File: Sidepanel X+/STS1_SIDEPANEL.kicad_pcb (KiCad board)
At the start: 2 copper layers, 82.8 x 100 mm, 39 parts, among them IC1 TMP112AQDRLRQ1, J1 Conn_01x08, U1 GUVA-C32SM, U11 INA180A4

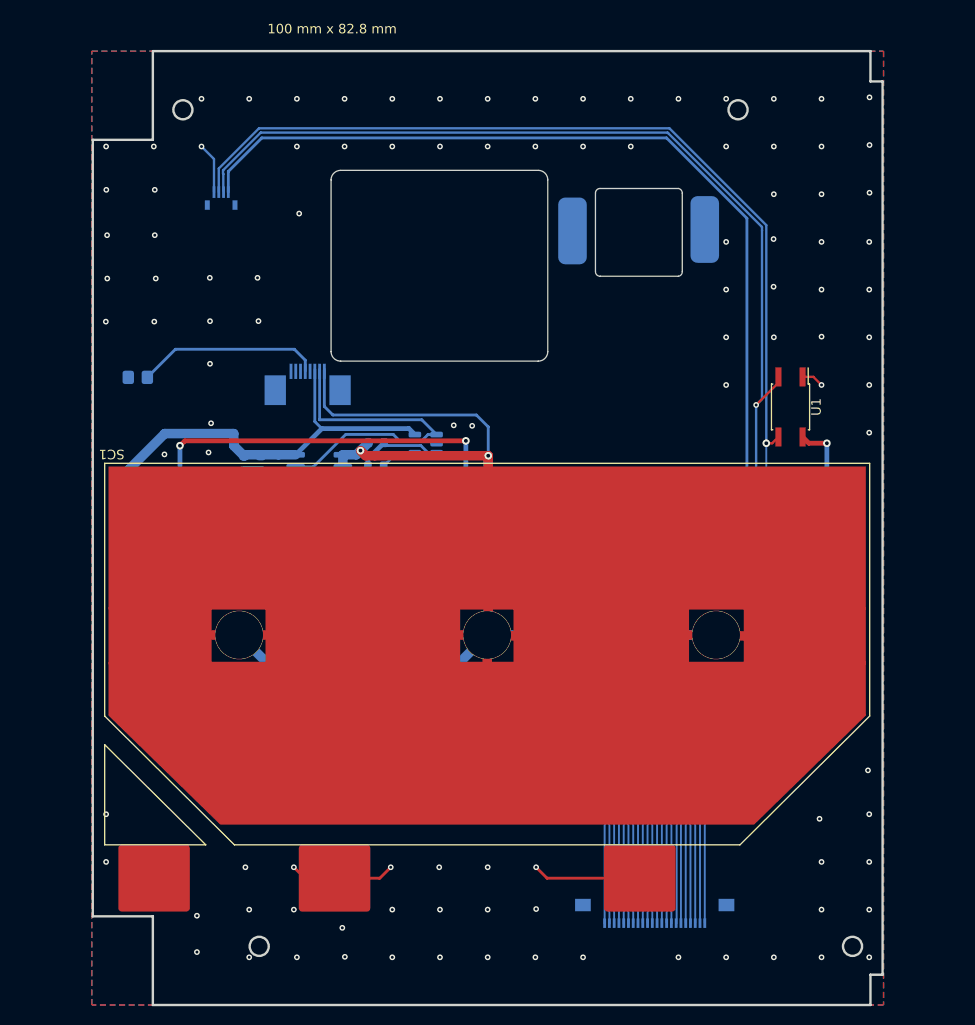
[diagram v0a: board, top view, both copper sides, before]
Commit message: fix for the issues: #19, #18 moved some components from the edge away to avoid collisions with the new structure
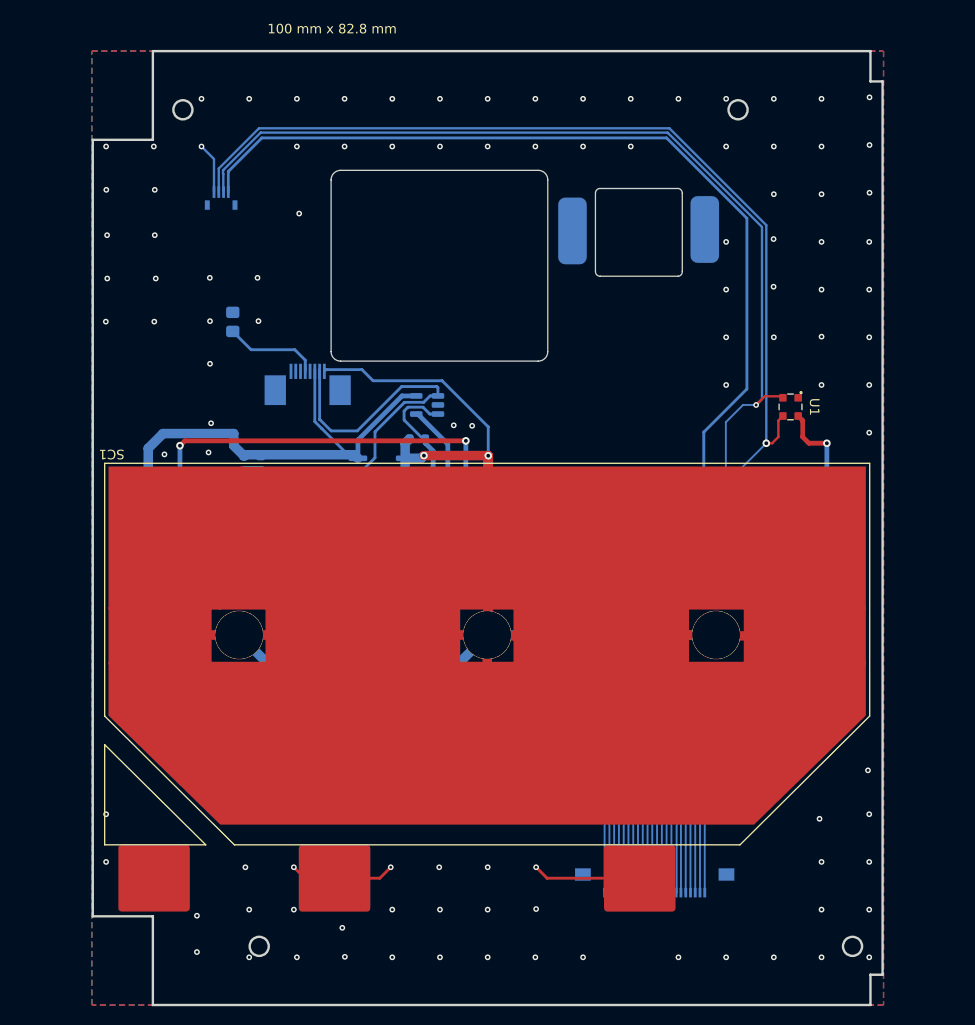
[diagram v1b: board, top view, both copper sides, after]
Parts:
- U1: footprint Package_SO:SO-4_4.4x3.6mm_P2.54mm -> STS_UV:OLGA 2mm x 2,3mm
- moved TH1 11.5 mm to (98.3, 67.9), turned to 90 degrees
- moved C_IN1 6.76 mm to (120.0, 85.5)
- moved R51 6.74 mm to (120.0, 83.5)
- moved CUR1 6.54 mm to (113.9, 84.1)
- moved C1 4.93 mm to (157.9, 94.6)
- moved RIC1 4.93 mm to (149.9, 89.3)
- moved RIC2 4.93 mm to (149.9, 91.3)
- moved RU1 4.93 mm to (149.9, 95.6)
- moved RU2 4.93 mm to (149.9, 93.6)
- moved C2 4.93 mm to (157.9, 90.4)
- moved IC1 4.93 mm to (154.3, 94.2)
- moved R41 4.33 mm to (117.6, 80.2)
- moved U11 4.05 mm to (118.7, 76.6)
- moved edu_con1 3.20 mm to (142.5, 125.7)
- moved C21 2.10 mm to (96.5, 94.5)
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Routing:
- net /TEMP+: track 19.4 -> 10.0 mm
- net /SC1_V+: track 213.6 -> 205.7 mm
- net /MPPT1: track 75.0 -> 82.1 mm
- net /SolarMPPT/CUR1_OUT(1): track 33.5 -> 38.8 mm
- net GND: track 57.5 -> 61.9 mm
- net Net-(cam1-Pad16): track 18.6 -> 15.4 mm
- net Net-(cam1-Pad9): track 18.6 -> 15.4 mm
- net Net-(cam1-Pad8): track 18.6 -> 15.4 mm
- net Net-(cam1-Pad7): track 18.6 -> 15.4 mm
- net Net-(cam1-Pad6): track 18.6 -> 15.4 mm
- net Net-(cam1-Pad5): track 18.6 -> 15.4 mm
- net Net-(cam1-Pad4): track 18.6 -> 15.4 mm
- net Net-(cam1-Pad3): track 18.6 -> 15.4 mm
- net Net-(cam1-Pad22): track 18.6 -> 15.4 mm
- net Net-(cam1-Pad21): track 18.6 -> 15.4 mm
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
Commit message: Changed the layout of all the sidepanel PCBs to mitigate the problems that arised from the bad previous design.
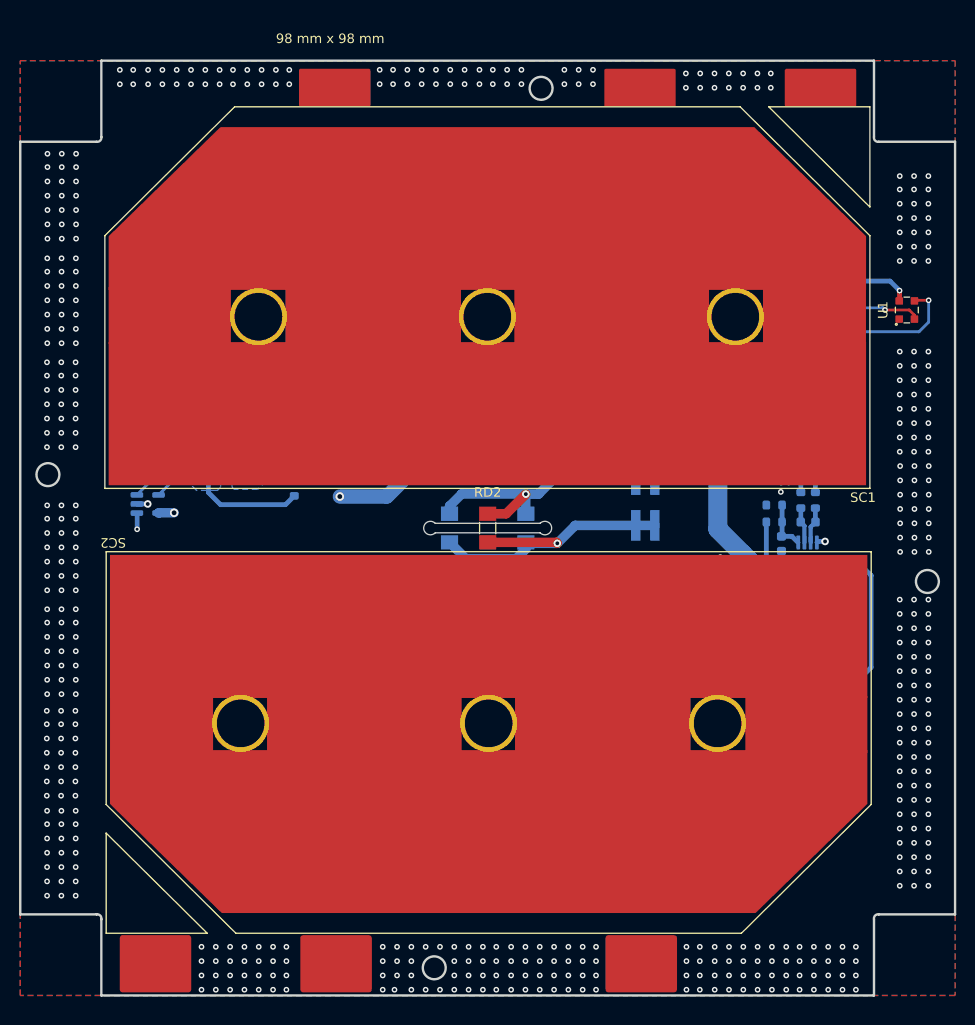
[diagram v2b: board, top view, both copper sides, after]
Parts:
- removed ? (x2): , 
- removed C2, CF1: 1u, Capacitor_SMD:C_0603_1608Metric
- removed COUT11: 4u7, Capacitor_SMD:C_0603_1608Metric
- removed COUT21, C_CUR21, C_IN1: 10u, Capacitor_SMD:C_0603_1608Metric
- removed CUR1: TMCS1101A3BQDT, Package_SO:SOIC-8_3.9x4.9mm_P1.27mm
- removed C_41, C_CUR11: 100n, Capacitor_SMD:C_0603_1608Metric
- removed D1: PMEG2020EH, Diode_SMD:D_SOD-123F
- removed DOUT1: SMM4F5.0, SamacSys:STMITE
- removed L_IN1: 10u, STS_Inductor_SMD:IND_XAL6060-103MEC
- removed RF11, RF21: 1k, Resistor_SMD:R_0603_1608Metric
- removed RIC1, RIC2: 4k7, Resistor_SMD:R_0603_1608Metric
- removed RS1: 0R01, Resistor_SMD:R_0603_1608Metric
- removed cam1, edu_con1: 54548-2271, STS_Connector:545482271
- added C11: 10u, Capacitor_SMD:C_0603_1608Metric, B.Cu at (95.4, 77.0)
- added C12: 10u, Capacitor_SMD:C_0603_1608Metric, B.Cu at (155.0, 104.4)
- added C22: 100n, Capacitor_SMD:C_0603_1608Metric, B.Cu at (161.9, 95.2)
- added C31: 1n, Capacitor_SMD:C_0603_1608Metric, B.Cu at (108.4, 77.8)
- added C32: 1n, Capacitor_SMD:C_0603_1608Metric, B.Cu at (155.8, 91.1)
- added C41: 4u7, Capacitor_SMD:C_0603_1608Metric, B.Cu at (101.3, 75.4)
- added C42: 1u, Capacitor_SMD:C_0603_1608Metric, B.Cu at (158.6, 88.9)
- added C51: 1u, Capacitor_SMD:C_0603_1608Metric, B.Cu at (111.4, 80.3)
- added C52: 4u7, Capacitor_SMD:C_0603_1608Metric, B.Cu at (153.5, 98.0)
- added C61: 10u, Capacitor_SMD:C_0603_1608Metric, B.Cu at (106.5, 73.1)
- added C62: 10u, Capacitor_SMD:C_0603_1608Metric, B.Cu at (151.5, 93.7)
- added D11: PMEG2020EH, Diode_SMD:D_SOD-123F, B.Cu at (101.6, 77.4)
- added D12: PMEG2020EH, Diode_SMD:D_SOD-123F, B.Cu at (155.5, 98.8)
- added D21: SMM4F5.0, STS_semiconductor:DIO_SMM4F5.0A-TR, B.Cu at (102.9, 73.3)
- added D22: SMM4F5.0, STS_semiconductor:DIO_SMM4F5.0A-TR, B.Cu at (151.5, 98.7)
- added J3: Conn_02x02_Odd_Even, STS_Connector:M808280442, B.Cu at (141.5, 86.8)
- added L1: 10u, STS_Inductor_SMD:IND_XAL6060-103MEC, B.Cu at (97.7, 82.2)
- added L_IN2: 10u, STS_Inductor_SMD:IND_XAL6060-103MEC, B.Cu at (160.4, 102.8)
- added MPPT2: SPV1040TTR, Package_SO:TSSOP-8_4.4x3mm_P0.65mm, B.Cu at (158.5, 93.9)
- added R12: 10m, Resistor_SMD:R_0603_1608Metric, B.Cu at (157.6, 107.9)
- added R22: 1k, Resistor_SMD:R_0603_1608Metric, B.Cu at (161.9, 93.7)
- added R32: 1k, Resistor_SMD:R_0603_1608Metric, B.Cu at (159.4, 86.6)
- added R42: 1k, Resistor_SMD:R_0603_1608Metric, B.Cu at (157.8, 86.6)
- added R52: 0R01, Resistor_SMD:R_0603_1608Metric, B.Cu at (153.8, 94.5)
- added R61: 1M, Resistor_SMD:R_0603_1608Metric, B.Cu at (111.0, 76.9)
- added R62: 1M, Resistor_SMD:R_0603_1608Metric, B.Cu at (155.0, 88.9)
- added R71: 330k, Resistor_SMD:R_0603_1608Metric, B.Cu at (112.5, 76.9)
- added R72: 330k, Resistor_SMD:R_0603_1608Metric, B.Cu at (155.0, 87.1)
- added RD1: 22R, Resistor_SMD:R_MiniMELF_MMA-0204, B.Cu at (121.0, 89.5)
- added RD2: 22R, Resistor_SMD:R_MiniMELF_MMA-0204, F.Cu at (125.0, 89.5)
- added RD3: 22R, Resistor_SMD:R_MiniMELF_MMA-0204, B.Cu at (129.0, 89.5)
- added SC2: Solar_Cell, STS_solder:3G30A_40x80_Z_SC2, F.Cu at (125.1, 112.0)
- added U12: INA180A4, Package_TO_SOT_SMD:SOT-23-5, B.Cu at (161.6, 111.2)
- C21: value 1n -> 100n
- J1: value Conn_01x08 -> Conn_01x10; footprint STS_Connector:SAMTEC_ZF5S-08-01-T-WT -> STS_connector:SAMTEC_ZF5S-08-01-T-WT
- Outline1: footprint USER_OUTLINE:OUTLINE_SidepanelX+ -> STS_Sidepanels_Outline:OUTLINE_SidepanelX+
- R11: value 1M -> 10m
- R21: value 330k -> 1k
- R41: value 0 -> 1k
- R51: value 10m -> 0R01
- SC1: footprint STS_solder:3G30A_40x80 -> STS_solder:3G30A_40x80_Z_SC1
- U1: footprint STS_UV:OLGA 2mm x 2,3mm -> STS_UV:OLGA
- UV1: footprint STS_Connector:5014610491 -> STS_connector:5014610491
- moved UV1 68.0 mm to (161.8, 75.8), turned to 0 degrees
- moved TH1 52.8 mm to (150.4, 76.1), turned to 0 degrees
- moved SC1 37.4 mm to (125.0, 65.3), turned to 0 degrees
- moved C1 32.2 mm to (163.1, 62.8)
- moved U11 31.1 mm to (89.4, 87.0), turned to 0 degrees
- moved RU2 30.6 mm to (162.3, 65.6)
- moved IC1 27.0 mm to (161.6, 68.2), turned to 90 degrees
- moved RU1 26.9 mm to (161.3, 71.2)
- moved J1 26.0 mm to (132.1, 75.0), turned to 0 degrees
- moved R51 16.7 mm to (105.4, 75.5), turned to 180 degrees
- moved R21 16.3 mm to (104.7, 85.3), turned to -90 degrees
- moved U1 15.9 mm to (168.9, 66.6), turned to 90 degrees
- moved C21 13.7 mm to (104.0, 83.0), turned to 180 degrees
- moved R11 12.8 mm to (92.2, 81.7), turned to 0 degrees
- moved MPPT1 11.6 mm to (106.0, 80.4), turned to 0 degrees
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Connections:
- C21 pad 1: Net-(C21-Pad1) -> GND
- C21 pad 2: GND -> Net-(MPPT1-MPP-SET)
- J1 pad S1: (no net) -> unconnected-(J1-Pin_9-PadS1)
- J1 pad S2: (no net) -> unconnected-(J1-Pin_10-PadS2)
- MPPT1 pad 1: Net-(C_41-Pad2) -> Net-(MPPT1-MPP-SET)
- MPPT1 pad 3: /SolarMPPT/MPPT1_IN -> Net-(D11-A)
- MPPT1 pad 5: Net-(C21-Pad1) -> Net-(MPPT1-VCTRL)
- MPPT1 pad 6: Net-(CF1-Pad1) -> Net-(MPPT1-ICTRL_MINUS)
- MPPT1 pad 7: Net-(CF1-Pad2) -> Net-(MPPT1-ICTRL_PLUS)
- MPPT1 pad 8: Net-(C_41-Pad2) -> Net-(MPPT1-MPP-SET)
- R11 pad 1: Net-(C21-Pad1) -> /SC1_V+
- R11 pad 2: /MPPT1 -> /SolarMPPT/CUR1_OUT
- R21 pad 1: GND -> Net-(MPPT1-MPP-SET)
- R21 pad 2: Net-(C21-Pad1) -> /SolarMPPT/CUR1_OUT
- R31 pad 1: Net-(C_41-Pad2) -> /SolarMPPT/MPPT1_OUT
- R31 pad 2: /SolarMPPT/CUR1_OUT(1) -> Net-(MPPT1-ICTRL_PLUS)
- R41 pad 1: /SC1_V+ -> /MPPT1
- R41 pad 2: /SolarMPPT/CUR1_OUT -> Net-(MPPT1-ICTRL_MINUS)
- R51 pad 1: /SolarMPPT/CUR1_OUT -> /MPPT1
- R51 pad 2: /SolarMPPT/CUR1_OUT(1) -> /SolarMPPT/MPPT1_OUT
- U11 pad 3: /SolarMPPT/CUR1_OUT -> /SC1_V+
- U11 pad 4: /SolarMPPT/CUR1_OUT(1) -> /SolarMPPT/CUR1_OUT
- UV1 pad 4: GND -> unconnected-(UV1-Pad4)
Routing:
- net /SC1_V+: track 205.7 -> 47.8 mm, vias 2 -> 0
- net /+3V3: track 137.0 -> 25.8 mm
- net /SCL: track 112.3 -> 21.2 mm
- net /SDA: track 113.3 -> 24.8 mm, vias 1 -> 2
- net /MPPT2: track 0.00 -> 77.8 mm, vias 0 -> 3
- net /SolarMPPT/MPPT1_OUT: track 86.7 -> 24.0 mm
- net /SC2_I+: track 0.00 -> 54.5 mm, vias 0 -> 2
- net /SC2_V+: track 0.00 -> 45.9 mm, vias 0 -> 1
- net GND: track 61.9 -> 21.7 mm, vias 105 -> 703
- net /SolarMPPT/CUR1_OUT(1): track 38.8 -> 0.00 mm
- net /AntennaDeployment/ANT_DEPLOY-: track 0.00 -> 31.5 mm, vias 0 -> 1
- net /AntennaDeployment/ANT_DEPLOY+: track 0.00 -> 30.4 mm, vias 0 -> 1
- net /SolarMPPT/CUR2_OUT: track 0.00 -> 21.9 mm
- net /SolarMPPT/MPPT1_IN: track 21.4 -> 0.00 mm
- net /SolarMPPT/MPPT2_OUT: track 0.00 -> 20.7 mm, vias 0 -> 2
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- added copper zone on B.Cu, net /MPPT1
- added copper zone on B.Cu, net /MPPT2
- added copper zone on B.Cu, net /SC1_V+
- added copper zone on B.Cu, net /SC2_V+
- added copper zone on B.Cu, net /SolarMPPT/CUR1_OUT
- added copper zone on B.Cu, net /SolarMPPT/CUR2_OUT
- added copper zone on B.Cu, net /SolarMPPT/MPPT2_OUT
- added copper zone on In1.Cu, net GND
- added copper zone on In2.Cu, net GND
- added copper zone on B.Cu, net Net-(D11-A)
- added copper zone on B.Cu, net Net-(D12-A)
- removed copper zone on B.Cu, net /SolarMPPT/MPPT1_IN
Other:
- board size 82.8 x 100 mm -> 98 x 98 mm
- copper layers 2 -> 4
- board text added: "98 mm x 98 mm"
- board text added: "Y"
- board text added: "Z"
- board text removed: "100 mm x 82.8 mm"

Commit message: Added a  separate ground for the EDU  sensors and did  some small changes for ordering.
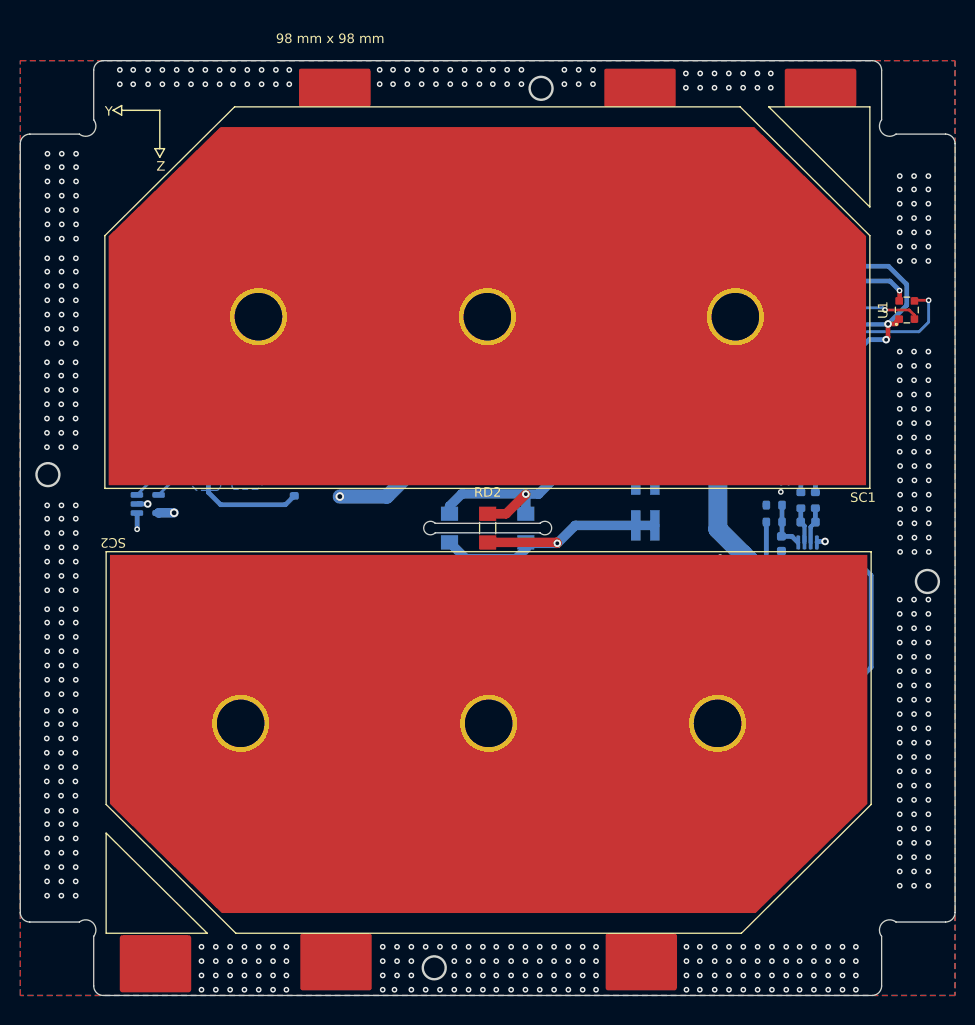
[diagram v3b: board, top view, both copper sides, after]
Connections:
- C1 pad 2: GND -> GND1
- IC1 pad 2: GND -> GND1
- IC1 pad 3: GND -> GND1
- U1 pad 1: GND -> GND1
- UV1 pad 4: unconnected-(UV1-Pad4) -> GND1
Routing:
- net GND1: track 0.00 -> 31.9 mm, vias 0 -> 2
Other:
- outline, holes or cut-outs redrawn

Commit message: Commit before the order.
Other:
- board text added: "V 2.5"
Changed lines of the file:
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@@
       (drillshape 0)
       (scaleselection 1)
-      (outputdirectory "../Gerber/Z-/")
+      (outputdirectory "../../gerber_SIDEPANELS/X+/")
     )
   )
@@
   (gr_line (start 83.7698 52.0982) (end 83.7698 51.5982)
     (stroke (width 0.15) (type default)) (layer "B.SilkS"))
-  (gr_line (start 86.629 45.7056) (end 90.629 45.7056)
-    (stroke (width 0.15) (type default)) (layer "F.SilkS"))
-  (gr_line (start 85.7314 45.7057) (end 86.629 46.2056)
-    (stroke (width 0.15) (type default)) (layer "F.SilkS"))
-  (gr_line (start 86.629 45.2056) (end 86.629 45.7056)
-    (stroke (width 0.15) (type default)) (layer "F.SilkS"))
-  (gr_line (start 86.629 45.7056) (end 86.629 46.2056)
-    (stroke (width 0.15) (type default)) (layer "F.SilkS"))
-  (gr_line (start 90.625 50.625) (end 91.1249 49.7274)
-    (stroke (width 0.15) (type default)) (layer "F.SilkS"))
-  (gr_line (start 90.625 50.625) (end 90.1249 49.7274)
-    (stroke (width 0.15) (type default)) (layer "F.SilkS"))
-  (gr_line (start 90.629 49.7056) (end 90.629 45.7056)
-    (stroke (width 0.15) (type default)) (layer "F.SilkS"))
-  (gr_line (start 90.6249 49.7274) (end 91.1249 49.7274)
-    (stroke (width 0.15) (type default)) (layer "F.SilkS"))
-  (gr_line (start 90.1249 49.7274) (end 90.6249 49.7274)
-    (stroke (width 0.15) (type default)) (layer "F.SilkS"))
-  (gr_line (start 85.7314 45.7057) (end 86.629 45.2056)
-    (stroke (width 0.15) (type default)) (layer "F.SilkS"))
   (gr_line (start 130.5 89) (end 119.5 89)
     (stroke (width 0.1) (type solid)) (layer "Edge.Cuts"))
@@
     (effects (font (size 1 1) (thickness 0.15)) (justify left bottom mirror))
   )
-  (gr_text "X+" (at 86.9 42.51 180) (layer "B.SilkS")
+  (gr_text "X+\n" (at 87.225 44.275 180) (layer "B.SilkS")
     (effects (font (size 1 1) (thickness 0.15)))
+  )
+  (gr_text "V 2.5" (at 88.375 46.525) (layer "B.SilkS")
+    (effects (font (size 1 1) (thickness 0.15)) (justify left bottom mirror))
   )
   (gr_text "98 mm x 98 mm" (at 108.49 38.192) (layer "F.SilkS")
     (effects (font (size 1 1) (thickness 0.15)))
   )
-  (gr_text "Y" (at 85.6974 46.3916) (layer "F.SilkS")
-    (effects (font (size 1 1) (thickness 0.15)) (justify right bottom))
-  )
-  (gr_text "Z" (at 91.2092 52.1574) (layer "F.SilkS")
-    (effects (font (size 1 1) (thickness 0.15)) (justify right bottom))
-  )
   (segment (start 109.2494 42.959) (end 109.0604 43.148) (width 0.5) (layer "F.Cu") (net 1))

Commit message: small changes before the order
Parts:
- removed C1: 1u, Capacitor_SMD:C_0603_1608Metric
- removed IC1: TMP112AQDRLRQ1, Package_TO_SOT_SMD:SOT-563
- removed RU1, RU2: 4k7, Resistor_SMD:R_0603_1608Metric
- removed U1: GUVA-C32SM, STS_UV:OLGA
- removed UV1: 501461-0491, STS_connector:5014610491
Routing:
- net GND1: track 31.9 -> 0.00 mm, vias 2 -> 0
- net /+3V3: track 25.8 -> 0.00 mm, vias 1 -> 0
- net /SDA: track 24.8 -> 0.00 mm, vias 2 -> 0
- net /SCL: track 21.2 -> 0.00 mm, vias 1 -> 0
